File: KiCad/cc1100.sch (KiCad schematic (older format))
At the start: 25 parts

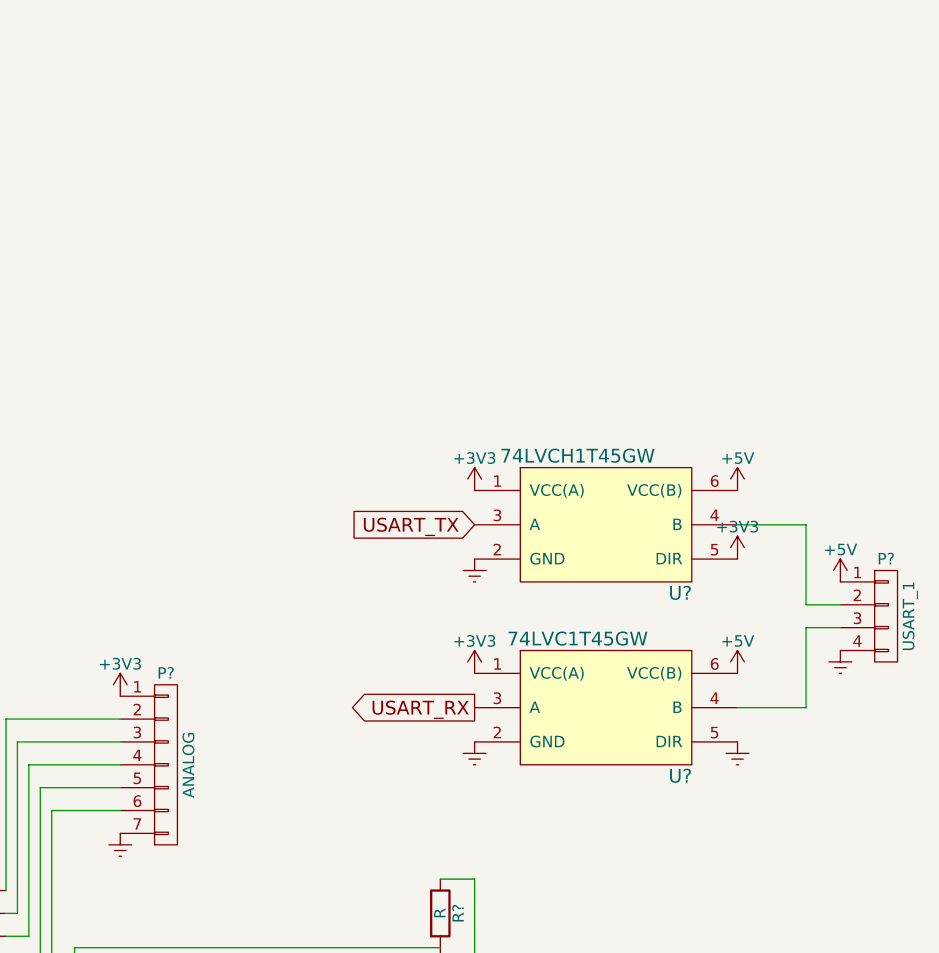
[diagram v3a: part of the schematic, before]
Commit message: Added decoupling for leveler
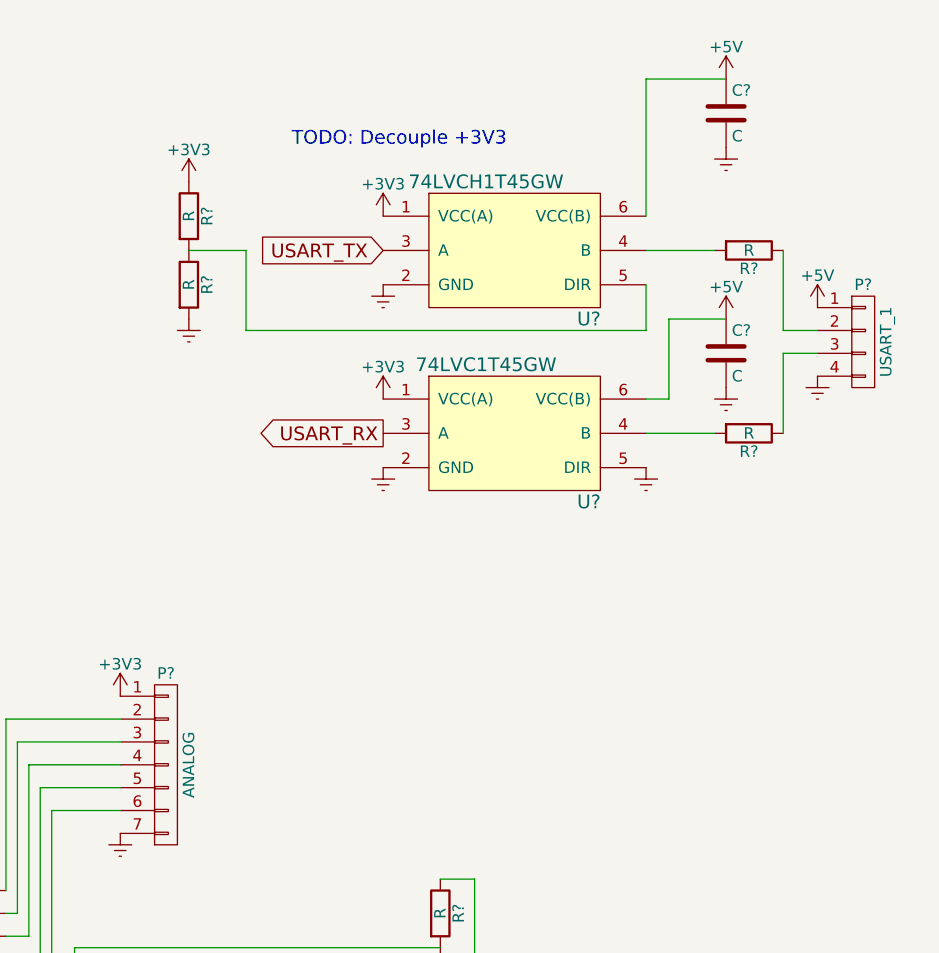
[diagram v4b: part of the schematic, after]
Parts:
- added C? (x2): C, symbol C
- added R? (x4): R, symbol R
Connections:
- net +3V3: now also R?.1; no longer U?.5 (DIR)
- net +5V: now also C?.1, C?.1
- net Earth: now also C?.2, C?.2, R?.2
- net at P?.2 (P2): now also R?.1; no longer U?.4 (B)
- net at P?.3 (P3): now also R?.1; no longer U?.4 (B)
- new net: R?.2, U?.4 (B) (x2)
- new net: R?.1, R?.2, U?.5 (DIR)
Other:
- note added: "TODO: Decouple +3V3"
- moved on the sheet: P?, U?

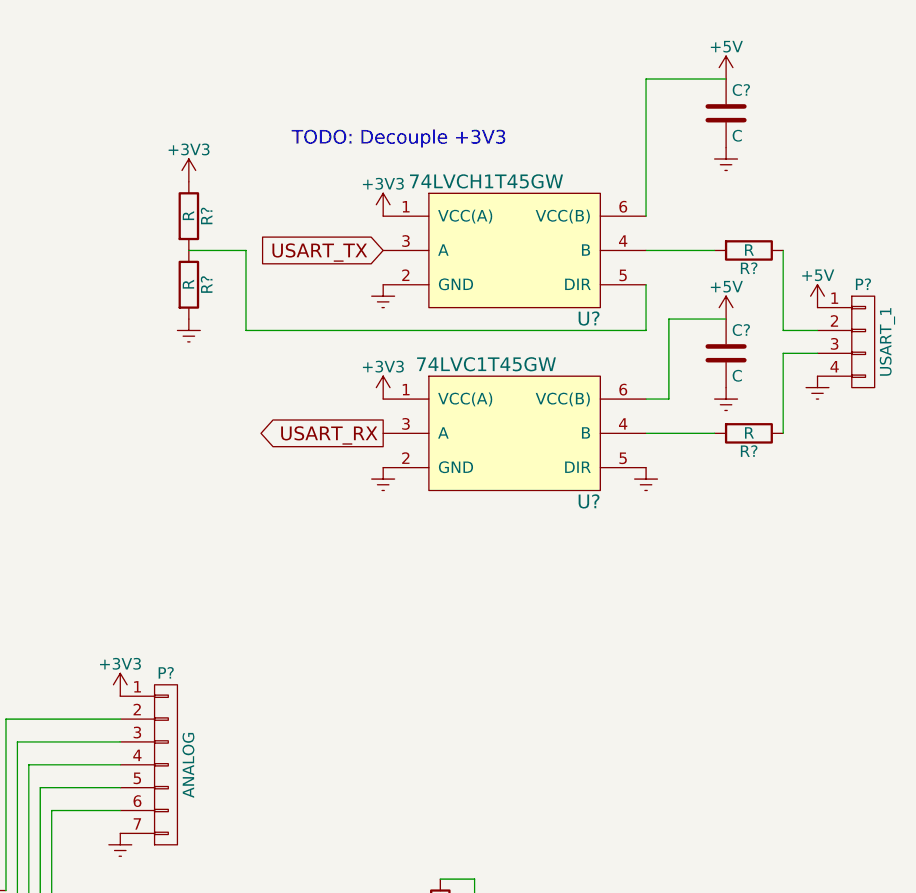
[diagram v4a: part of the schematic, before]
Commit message: Decoupled levelers
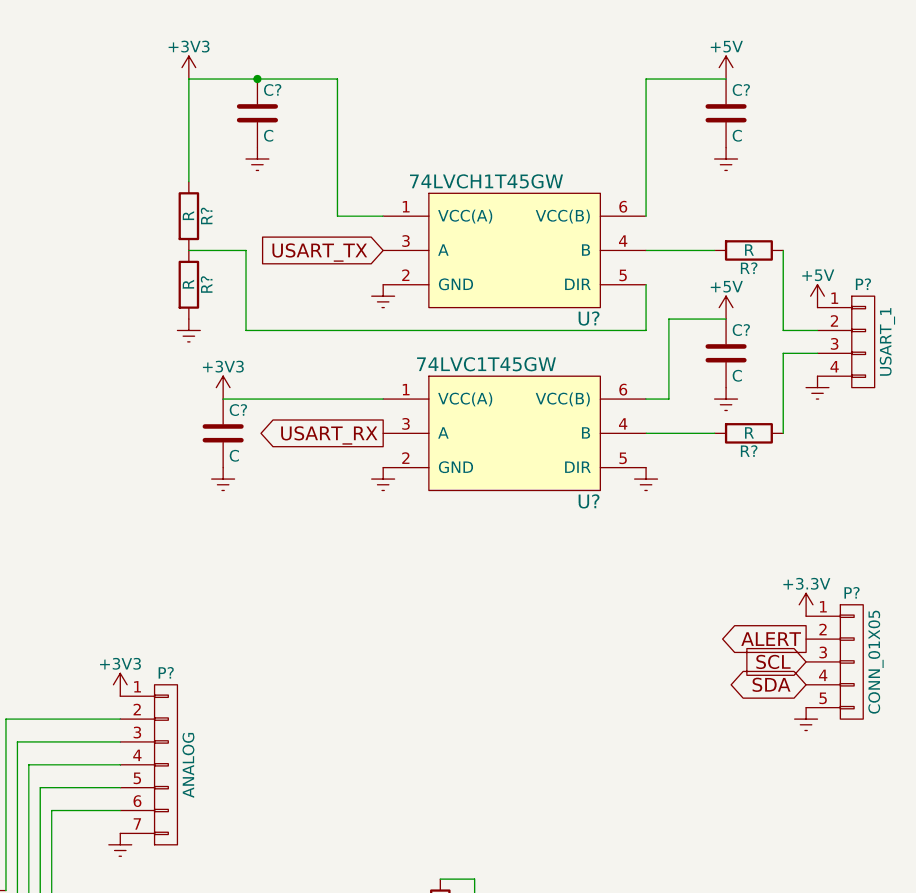
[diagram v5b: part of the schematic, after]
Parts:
- added C? (x2): C, symbol C
- added P?: CONN_01X05, symbol CONN_01X05
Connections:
- net +3V3: now also C?.1, C?.1, P?.1 (P1)
- net ALERT: now also P?.2 (P2)
- net Earth: now also C?.2, C?.2, P?.5 (P5)
- net SCL: now also P?.3 (P3)
- net SDA: now also P?.4 (P4)
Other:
- note removed: "TODO: Decouple +3V3"
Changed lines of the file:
@@
-$Comp
-L +3V3 #PWR?
-U 1 1 581E40D0
-P 8800 1400
-F 0 "#PWR?" H 8800 1250 50  0001 C CNN
-F 1 "+3V3" H 8800 1540 50  0000 C CNN
-F 2 "" H 8800 1400 50  0000 C CNN
-F 3 "" H 8800 1400 50  0000 C CNN
-	1    8800 1400
-	1    0    0    -1
-$EndComp
 $Comp
 L +3V3 #PWR?
 U 1 1 581E4148
-P 8800 2200
-F 0 "#PWR?" H 8800 2050 50  0001 C CNN
-F 1 "+3V3" H 8800 2340 50  0000 C CNN
-F 2 "" H 8800 2200 50  0000 C CNN
-F 3 "" H 8800 2200 50  0000 C CNN
-	1    8800 2200
+P 8100 2200
+F 0 "#PWR?" H 8100 2050 50  0001 C CNN
+F 1 "+3V3" H 8100 2340 50  0000 C CNN
+F 2 "" H 8100 2200 50  0000 C CNN
+F 3 "" H 8100 2200 50  0000 C CNN
+	1    8100 2200
 	1    0    0    -1
 $EndComp
@@
 L +3V3 #PWR?
 U 1 1 581EC55A
-P 7950 1250
-F 0 "#PWR?" H 7950 1100 50  0001 C CNN
-F 1 "+3V3" H 7950 1390 50  0000 C CNN
-F 2 "" H 7950 1250 50  0000 C CNN
-F 3 "" H 7950 1250 50  0000 C CNN
-	1    7950 1250
+P 7950 800
+F 0 "#PWR?" H 7950 650 50  0001 C CNN
+F 1 "+3V3" H 7950 940 50  0000 C CNN
+F 2 "" H 7950 800 50  0000 C CNN
+F 3 "" H 7950 800 50  0000 C CNN
+	1    7950 800
 	1    0    0    -1
 $EndComp
@@
 Wire Wire Line
 	8200 1550 7950 1550
-Text Notes 8400 1100 0    60   ~ 0
-TODO: Decouple +3V3
+$Comp
+L C C?
+U 1 1 581F736D
+P 8250 950
+F 0 "C?" H 8275 1050 50  0000 L CNN
+F 1 "C" H 8275 850 50  0000 L CNN
+F 2 "" H 8288 800 50  0000 C CNN
+F 3 "" H 8250 950 50  0000 C CNN
+	1    8250 950
+	1    0    0    -1
+$EndComp
+$Comp
+L Earth #PWR?
+U 1 1 581F7598
+P 8250 1100
+F 0 "#PWR?" H 8250 850 50  0001 C CNN
+F 1 "Earth" H 8250 950 50  0001 C CNN
+F 2 "" H 8250 1100 50  0000 C CNN
+F 3 "" H 8250 1100 50  0000 C CNN
+	1    8250 1100
+	1    0    0    -1
+$EndComp
+Wire Wire Line
+	7950 800  8600 800
+Wire Wire Line
+	8800 1400 8600 1400
+Wire Wire Line
+	8600 1400 8600 800
+Connection ~ 8250 800
+Wire Wire Line
+	7950 1250 7950 800
+$Comp
+L CONN_01X05 P?
+U 1 1 581F79D7
+P 10850 3350
+F 0 "P?" H 10850 3650 50  0000 C CNN
+F 1 "CONN_01X05" V 10950 3350 50  0000 C CNN
+F 2 "" H 10850 3350 50  0000 C CNN
+F 3 "" H 10850 3350 50  0000 C CNN
+	1    10850 3350
+	1    0    0    -1
+$EndComp
+$Comp
+L Earth #PWR?
+U 1 1 581F7A3D
+P 10650 3550
+F 0 "#PWR?" H 10650 3300 50  0001 C CNN
+F 1 "Earth" H 10650 3400 50  0001 C CNN
+F 2 "" H 10650 3550 50  0000 C CNN
+F 3 "" H 10650 3550 50  0000 C CNN
+	1    10650 3550
+	1    0    0    -1
+$EndComp
+$Comp
+L +3.3V #PWR?
+U 1 1 581F7A93
+P 10650 3150
+F 0 "#PWR?" H 10650 3000 50  0001 C CNN
+F 1 "+3.3V" H 10650 3290 50  0000 C CNN
+F 2 "" H 10650 3150 50  0000 C CNN
+F 3 "" H 10650 3150 50  0000 C CNN
+	1    10650 3150
+	1    0    0    -1
+$EndComp
+Text GLabel 10650 3250 0    60   Output ~ 0
+ALERT
+Text GLabel 10650 3350 0    60   Input ~ 0
+SCL
+Text GLabel 10650 3450 0    60   BiDi ~ 0
+SDA
+$Comp
+L C C?
+U 1 1 581F7D9B
+P 8100 2350
+F 0 "C?" H 8125 2450 50  0000 L CNN
+F 1 "C" H 8125 2250 50  0000 L CNN
+F 2 "" H 8138 2200 50  0000 C CNN
+F 3 "" H 8100 2350 50  0000 C CNN
+	1    8100 2350
+	1    0    0    -1
+$EndComp
+$Comp
+L Earth #PWR?
+U 1 1 581F7E82
+P 8100 2500
+F 0 "#PWR?" H 8100 2250 50  0001 C CNN
+F 1 "Earth" H 8100 2350 50  0001 C CNN
+F 2 "" H 8100 2500 50  0000 C CNN
+F 3 "" H 8100 2500 50  0000 C CNN
+	1    8100 2500
+	1    0    0    -1
+$EndComp
+Wire Wire Line
+	8100 2200 8800 2200
 $EndSCHEMATC

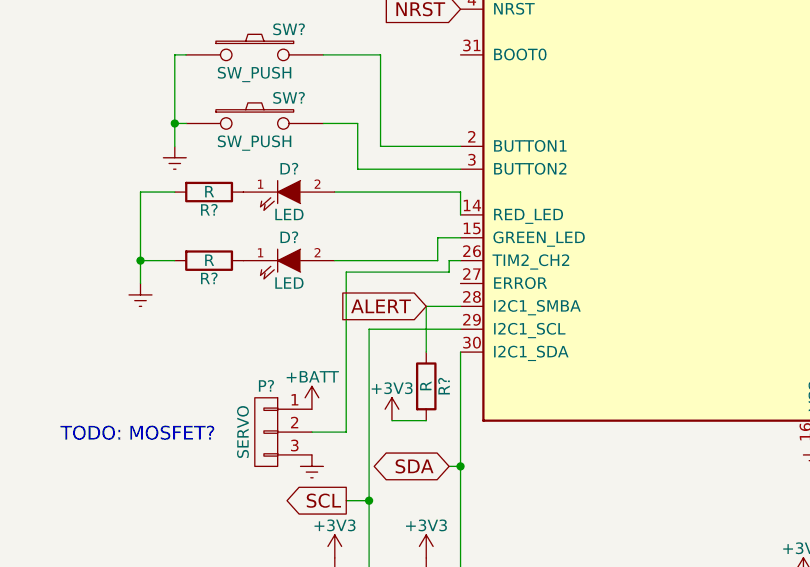
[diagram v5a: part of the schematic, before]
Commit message: Connected supply error pin
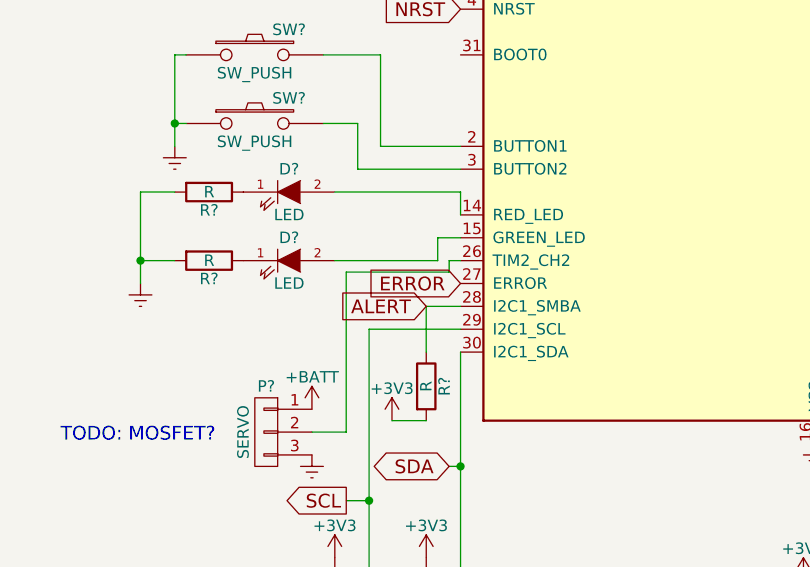
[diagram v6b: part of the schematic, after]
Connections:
- net ERROR: now reaches U?.27 (ERROR)
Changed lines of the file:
@@
 Wire Wire Line
 	8100 2200 8800 2200
+Text GLabel 3800 5600 0    60   Input ~ 0
+ERROR
 $EndSCHEMATC

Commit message: KiCad Update and ALERT pull-up added
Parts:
- added JP?: I2C_PULL_3, symbol JUMPER3
- D? (x2): symbol LED -> LED-RESCUE-cc1100
- P?: symbol USB_OTG -> USB_OTG-RESCUE-cc1100
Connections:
- net +3V3: now also R?.1; no longer R?.2
- net ALERT: now also JP?.2; no longer R?.1
- new net: JP?.3, R?.2
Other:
- moved on the sheet: P?, R?
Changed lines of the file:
@@
 EESchema Schematic File Version 2
+LIBS:cc1100-rescue
 LIBS:power
 LIBS:device
@@
 $EndComp
 $Comp
-L USB_OTG P?
+L USB_OTG-RESCUE-cc1100 P?
 U 1 1 58100E6C
 P 9600 5450
@@
 $EndComp
 $Comp
-L LED D?
+L LED-RESCUE-cc1100 D?
 U 1 1 5810D45B
 P 3050 5200
@@
 $EndComp
 $Comp
-L LED D?
+L LED-RESCUE-cc1100 D?
 U 1 1 5810D4C6
 P 3050 5500
@@
 L R R?
 U 1 1 581106B3
-P 3650 6050
-F 0 "R?" V 3730 6050 50  0000 C CNN
-F 1 "R" V 3650 6050 50  0000 C CNN
-F 2 "" V 3580 6050 50  0000 C CNN
-F 3 "" H 3650 6050 50  0000 C CNN
-	1    3650 6050
+P 4250 6950
+F 0 "R?" V 4330 6950 50  0000 C CNN
+F 1 "R" V 4250 6950 50  0000 C CNN
+F 2 "" V 4180 6950 50  0000 C CNN
+F 3 "" H 4250 6950 50  0000 C CNN
+	1    4250 6950
 	1    0    0    -1
 $EndComp
@@
 L +3V3 #PWR?
 U 1 1 5811071B
-P 3500 6200
-F 0 "#PWR?" H 3500 6050 50  0001 C CNN
-F 1 "+3V3" H 3500 6340 50  0000 C CNN
-F 2 "" H 3500 6200 50  0000 C CNN
-F 3 "" H 3500 6200 50  0000 C CNN
-	1    3500 6200
-	1    0    0    -1
-$EndComp
-Text GLabel 3650 5700 0    60   Input ~ 0
+P 4250 6800
+F 0 "#PWR?" H 4250 6650 50  0001 C CNN
+F 1 "+3V3" H 4250 6940 50  0000 C CNN
+F 2 "" H 4250 6800 50  0000 C CNN
+F 3 "" H 4250 6800 50  0000 C CNN
+	1    4250 6800
+	1    0    0    -1
+$EndComp
+Text GLabel 4250 6450 0    60   Input ~ 0
 ALERT
-Wire Wire Line
-	3500 6200 3650 6200
-Wire Wire Line
-	3650 5900 3650 5700
-Wire Wire Line
-	3650 5700 3800 5700
 $Comp
 L 74LVCH1T45GW U?
@@
 L CONN_01X05 P?
 U 1 1 581F79D7
-P 10850 3350
-F 0 "P?" H 10850 3650 50  0000 C CNN
-F 1 "CONN_01X05" V 10950 3350 50  0000 C CNN
-F 2 "" H 10850 3350 50  0000 C CNN
-F 3 "" H 10850 3350 50  0000 C CNN
-	1    10850 3350
+P 2400 7100
+F 0 "P?" H 2400 7400 50  0000 C CNN
+F 1 "CONN_01X05" V 2500 7100 50  0000 C CNN
+F 2 "" H 2400 7100 50  0000 C CNN
+F 3 "" H 2400 7100 50  0000 C CNN
+	1    2400 7100
 	1    0    0    -1
 $EndComp
@@
 L Earth #PWR?
 U 1 1 581F7A3D
-P 10650 3550
-F 0 "#PWR?" H 10650 3300 50  0001 C CNN
-F 1 "Earth" H 10650 3400 50  0001 C CNN
-F 2 "" H 10650 3550 50  0000 C CNN
-F 3 "" H 10650 3550 50  0000 C CNN
-	1    10650 3550
+P 2200 7300
+F 0 "#PWR?" H 2200 7050 50  0001 C CNN
+F 1 "Earth" H 2200 7150 50  0001 C CNN
+F 2 "" H 2200 7300 50  0000 C CNN
+F 3 "" H 2200 7300 50  0000 C CNN
+	1    2200 7300
 	1    0    0    -1
 $EndComp
@@
 L +3.3V #PWR?
 U 1 1 581F7A93
-P 10650 3150
-F 0 "#PWR?" H 10650 3000 50  0001 C CNN
-F 1 "+3.3V" H 10650 3290 50  0000 C CNN
-F 2 "" H 10650 3150 50  0000 C CNN
-F 3 "" H 10650 3150 50  0000 C CNN
-	1    10650 3150
-	1    0    0    -1
-$EndComp
-Text GLabel 10650 3250 0    60   Output ~ 0
+P 2200 6900
+F 0 "#PWR?" H 2200 6750 50  0001 C CNN
+F 1 "+3.3V" H 2200 7040 50  0000 C CNN
+F 2 "" H 2200 6900 50  0000 C CNN
+F 3 "" H 2200 6900 50  0000 C CNN
+	1    2200 6900
+	1    0    0    -1
+$EndComp
+Text GLabel 2200 7000 0    60   Output ~ 0
 ALERT
-Text GLabel 10650 3350 0    60   Input ~ 0
+Text GLabel 2200 7100 0    60   Input ~ 0
 SCL
-Text GLabel 10650 3450 0    60   BiDi ~ 0
+Text GLabel 2200 7200 0    60   BiDi ~ 0
 SDA
 $Comp
@@
 Text GLabel 3800 5600 0    60   Input ~ 0
 ERROR
+$Comp
+L JUMPER3 JP?
+U 1 1 58C87A94
+P 4250 7350
+F 0 "JP?" H 4300 7250 50  0000 L CNN
+F 1 "I2C_PULL_3" H 4250 7450 50  0000 C BNN
+F 2 "" H 4250 7350 50  0000 C CNN
+F 3 "" H 4250 7350 50  0000 C CNN
+	1    4250 7350
+	0    -1   -1   0
+$EndComp
+Wire Wire Line
+	4350 6300 4350 7350
+Wire Wire Line
+	4350 6450 4250 6450
+Wire Wire Line
+	3800 5700 3750 5700
+Wire Wire Line
+	3750 5700 3750 6300
+Wire Wire Line
+	3750 6300 4350 6300
+Connection ~ 4350 6450
 $EndSCHEMATC
